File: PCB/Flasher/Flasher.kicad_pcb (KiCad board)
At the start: 2 copper layers, 70 x 70 mm, 48 parts, among them J1 1x5, J2 TC2030-USB-NL, J3 Reset, Q1 BSS138PS, U1 TPS562246, U4 ESP32-S3-MINI-1

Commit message: Start PCb
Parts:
- removed D2, D3: ~, RevK:DFN1006-2L
- removed D4: D, RevK:D_0402
- removed J1: 1x5, RevK:JST_EH_S5B-EH_1x05_P2.50mm_Horizontal
- removed J2: TC2030-USB-NL, RevK:Tag-Connect_TC2030-IDC-NL_2x03_P1.27mm_Vertical
- removed Q1: BSS138PS, RevK:SOT-363_SC-70-6
- removed R1, R2: 10k, RevK:R_0201
- removed TP1: TestPoint, RevK:1x2-Hole
- removed V1, V2: ~, RevK:VCUT70N
- J3, TP10, TP2, TP3, TP4, TP5, TP6, TP7, TP8, TP9, V6: moved to F.Cu
- moved J3 69.7 mm to (195.2, 40.9), turned to 0 degrees
- moved FID3 67.6 mm to (190.2, 44.7)
- moved U4 65.4 mm to (185.6, 31.0), turned to 0 degrees
- moved FID2 62.1 mm to (190.2, 41.2)
- moved R8 54.0 mm to (187.5, 43.1), turned to 0 degrees
- moved R6 54.0 mm to (187.5, 41.6), turned to 0 degrees
- moved R5 53.6 mm to (187.5, 40.1), turned to 0 degrees
- moved C2 53.3 mm to (182.0, 41.6), turned to 0 degrees
- moved TP6 52.9 mm to (176.6, 43.9)
- moved TP8 52.5 mm to (179.6, 40.9)
- moved TP5 51.8 mm to (176.6, 40.9)
- moved C19 51.8 mm to (185.7, 41.6), turned to 0 degrees
- moved C18 51.5 mm to (185.7, 40.1), turned to 0 degrees
- moved TP4 50.5 mm to (173.6, 46.9)
- moved C1 50.2 mm to (182.0, 40.1), turned to 0 degrees
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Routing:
- net +3.3V: track 66.0 -> 0.00 mm, vias 6 -> 0
- net D+: track 44.5 -> 0.00 mm, vias 3 -> 0
- net Net-(J1-Pin_3): track 43.6 -> 0.00 mm
- net D-: track 40.2 -> 0.00 mm, vias 3 -> 0
- net DC: track 38.8 -> 0.00 mm, vias 3 -> 0
- net Net-(D4-K): track 36.0 -> 0.00 mm, vias 4 -> 0
- net RST: track 19.8 -> 0.00 mm, vias 2 -> 0
- net GND: track 10.8 -> 0.00 mm, vias 52 -> 0
- net SW: track 9.82 -> 0.00 mm, vias 2 -> 0
- net RX: track 8.62 -> 0.00 mm, vias 1 -> 0
- net Net-(J3-Pin_2): track 7.03 -> 0.00 mm, vias 1 -> 0
- net TX: track 6.23 -> 0.00 mm, vias 1 -> 0
- net FB: track 2.64 -> 0.00 mm
- net LED: track 2.56 -> 0.00 mm
- net Net-(J1-Pin_1): track 2.22 -> 0.00 mm
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- removed copper zone on B.Cu, net GND
- removed copper zone on F.Cu, net GND
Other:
- board text removed: "${CURRENT_DATE}"
- board text removed: "+"
- board text removed: "-"
- board text removed: "1"
- board text removed: "12V"
- board text removed: "21"
- board text removed: "3"
- board text removed: "34"
- board text removed: "3V3"
- board text removed: "47"
- board text removed: "48"
- board text removed: "5"
- board text removed: "5V"
- board text removed: "6 V-cuts"
- board text removed: "<"
- board text removed: ">"
- board text removed: "A"
- board text removed: "D+"
- board text removed: "D-"
- board text removed: "Designed by RevK www.me.uk"
- board text removed: "EN"
- board text removed: "F"
- board text removed: "Made in China for Andrews & Arnold Ltd"
- board text removed: "RX"
- board text removed: "S21"
- board text removed: "TX"
- board text removed: "U"
- board text removed: "aikin"
- board text removed: "aikin.uk"
- board text removed: "www.f"
- board text removed: "®"
- board text removed: "⏚"

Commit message: Parts
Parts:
- removed C17: 22uF 25V, RevK:C_0805
- removed C18: 100nF, RevK:C_0201
- removed C19: 18pF, RevK:C_0201
- removed FID3: Fiducial, Fiducial:Fiducial_1mm_Mask2mm
- removed TP10, TP2, TP3, TP4, TP5, TP6, TP7, TP8, TP9: TestPoint, RevK:PAD-2mm
- removed V5, V6: ~, RevK:VCUT70N
- added C10: 100nF, RevK:C_0201, F.Cu at (197.9, 49.8)
- added C11: 100nF, RevK:C_0201, F.Cu at (199.8, 46.8)
- added C12: 100nF, RevK:C_0201, F.Cu at (199.8, 48.3)
- added C13: 100nF, RevK:C_0402, F.Cu at (203.9, 52.8)
- added C14: 100nF, RevK:C_0201, F.Cu at (175.2, 58.5)
- added C8: 100nF, RevK:C_0201, F.Cu at (197.9, 46.8)
- added C9: 100nF, RevK:C_0201, F.Cu at (197.9, 48.3)
- added D10: XL-1010RGBC-WS2812B, RevK:SMD1010, F.Cu at (214.1, 53.1)
- added D2: XL-1010RGBC-WS2812B, RevK:SMD1010, F.Cu at (209.4, 47.5)
- added D3: XL-1010RGBC-WS2812B, RevK:SMD1010, F.Cu at (211.7, 47.5)
- added D4: XL-1010RGBC-WS2812B, RevK:SMD1010, F.Cu at (214.1, 47.5)
- added D5: XL-1010RGBC-WS2812B, RevK:SMD1010, F.Cu at (209.4, 50.3)
- added D6: XL-1010RGBC-WS2812B, RevK:SMD1010, F.Cu at (211.7, 50.3)
- added D7: XL-1010RGBC-WS2812B, RevK:SMD1010, F.Cu at (214.1, 50.3)
- added D8: XL-1010RGBC-WS2812B, RevK:SMD1010, F.Cu at (209.4, 53.1)
- added D9: XL-1010RGBC-WS2812B, RevK:SMD1010, F.Cu at (211.7, 53.1)
- added FID1: Fiducial, Fiducial:Fiducial_1mm_Mask2mm, F.Cu at (198.8, 52.4)
- added J1: Reset, RevK:AA-Pad, F.Cu at (188.0, 47.6)
- added J2: Wago, RevK:WAGO-2060-453-998-404, F.Cu at (179.6, 48.8)
- added J4: USB-C-Socket-V, RevK:USB-C-Socket-H, F.Cu at (211.2, 61.8)
- added J5: TF_PUSH, RevK:TF_PUSH, F.Cu at (206.9, 80.4)
- added R1: 150k 1%, RevK:R_0201, F.Cu at (199.8, 49.8)
- added R10: 27R, RevK:R_0201, F.Cu at (216.7, 73.5)
- added R11: 10K, RevK:R_0201, F.Cu at (216.7, 75.0)
- added R12: 10K, RevK:R_0201, F.Cu at (216.7, 76.5)
- added R13: 10K, RevK:R_0201, F.Cu at (216.7, 78.0)
- added R14: 10K, RevK:R_0201, F.Cu at (216.7, 79.5)
- added R15: 10K, RevK:R_0201, F.Cu at (216.7, 81.0)
- added R2: 10K, RevK:R_0201, F.Cu at (201.6, 46.8)
- added R4: 33k 1%, RevK:R_0201, F.Cu at (201.6, 48.3)
- added R7: 5K1, RevK:R_0201, F.Cu at (201.6, 49.8)
- added R9: 27R, RevK:R_0201, F.Cu at (216.7, 72.0)
- added U2: TPS562246, RevK:SOT-563, F.Cu at (204.5, 47.6)
- added U3: FT231XQ, RevK:QFN-20-1EP_4x4mm_P0.5mm_EP2.5x2.5mm, F.Cu at (194.1, 49.0)
- added V1: ~, RevK:VCUT70N, F.Cu at (209.4, 37.2)
- added V2: ~, RevK:VCUT70N, F.Cu at (209.4, 39.7)
- C1: value 100nF -> 22uF 25V; footprint RevK:C_0201 -> RevK:C_0805
- C15: value 47uF 6V -> 100nF; footprint RevK:C_0805 -> RevK:C_0201
- C16: value 100nF 25V -> 100nF; footprint RevK:C_0402 -> RevK:C_0201
- C2: value 100nF -> 100nF 25V; footprint RevK:C_0201 -> RevK:C_0402
- C4: value 100nF -> 1uF
- C6: value 1uF -> 18pF
- C7: value 100nF -> 47uF 6V; footprint RevK:C_0201 -> RevK:C_0805
- J3: value Reset -> Wago; footprint RevK:AA-Pad -> RevK:WAGO-2060-453-998-404
- R3: value 10K -> 150k 1%
- R5, R6: value 150k 1% -> 10K
- R8: value 33k 1% -> 5K1
- U1: value TPS562246 -> ESP32-S3-MINI-1; footprint RevK:SOT-563 -> RevK:ESP32-S3-MINI-1
- U4: value ESP32-S3-MINI-1 -> TPS22916CNYFPR; footprint RevK:ESP32-S3-MINI-1 -> RevK:WCSP-4-0.78x0.78
- moved V3 96.4 mm to (209.5, 32.0)
- moved V4 96.4 mm to (209.5, 34.4)
- moved U4 50.2 mm to (175.7, 80.2)
- moved U1 32.3 mm to (187.6, 82.2)
- moved C3 21.1 mm to (182.8, 70.4)
- moved C1 21.1 mm to (181.4, 61.2)
- moved C2 21.1 mm to (181.4, 62.8)
- moved C4 21.1 mm to (181.4, 64.2)
- moved C5 21.1 mm to (183.2, 61.2)
- moved C6 21.1 mm to (183.2, 62.8)
- moved C7 21.1 mm to (183.2, 64.2)
- moved D1 21.1 mm to (185.2, 74.0)
- moved FID2 21.1 mm to (189.6, 62.3)
- moved J3 21.1 mm to (194.6, 62.0)
- moved L1 21.1 mm to (174.5, 72.6)
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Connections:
- C1 pad 1: GND -> DC
- C1 pad 2: +3.3V -> GND
- C16 pad 1: DC -> +3.3V
- C2 pad 1: GND -> DC
- C2 pad 2: +3.3V -> GND
- C4 pad 1: GND -> RST
- C4 pad 2: +3.3V -> GND
- C5 pad 1: GND -> BST
- C5 pad 2: +3.3V -> SW
- C6 pad 1: RST -> FB
- C6 pad 2: GND -> +3.3V
- C7 pad 1: GND -> +3.3V
- C7 pad 2: +3.3V -> GND
- D1 pad 1: unconnected-(D1-O-Pad1) -> Net-(D1-O)
- J3 pad 1: GND -> Net-(J3-Pin_1)
- J3 pad 2: Net-(J3-Pin_2) -> Net-(J2-Pin_3)
- R3 pad 2: RST -> FB
- R5 pad 1: EN -> +3.3V
- R5 pad 2: DC -> SDCD
- R6 pad 2: FB -> SDDAT1
- R8 pad 1: FB -> GND
- R8 pad 2: GND -> Net-(J4-CC2)
- U1 pad 1: DC -> GND
- U1 pad 2: SW -> GND
- U1 pad 3: GND -> +3.3V
- U1 pad 4: BST -> GPIO0
- U1 pad 5: EN -> unconnected-(U1-GPIO1-Pad5)
- U1 pad 6: FB -> unconnected-(U1-GPIO2-Pad6)

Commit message: Started placement
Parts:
- removed FID1, FID2: Fiducial, Fiducial:Fiducial_1mm_Mask2mm
- removed V1, V4: ~, RevK:VCUT70N
- moved D4 94.5 mm to (124.0, 76.0)
- moved D3 94.1 mm to (122.0, 76.0)
- moved D2 93.8 mm to (120.0, 76.0)
- moved R15 92.2 mm to (125.0, 71.5), turned to -90 degrees
- moved R14 90.6 mm to (126.5, 71.5), turned to -90 degrees
- moved R13 89.0 mm to (128.0, 71.5), turned to -90 degrees
- moved D7 87.9 mm to (130.0, 76.0)
- moved D6 87.6 mm to (128.0, 76.0)
- moved R12 87.4 mm to (129.5, 71.5), turned to -90 degrees
- moved D5 87.3 mm to (126.0, 76.0)
- moved J3 86.6 mm to (108.5, 71.5)
- moved R11 85.8 mm to (131.0, 71.5), turned to -90 degrees
- moved R10 84.2 mm to (132.5, 71.5), turned to -90 degrees
- moved V2 83.7 mm to (135.0, 78.0), turned to 180 degrees
- moved R9 82.7 mm to (134.0, 71.5), turned to -90 degrees
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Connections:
- J2 pad 3: Net-(J2-Pin_3) -> LOOP
- J3 pad 2: Net-(J2-Pin_3) -> LOOP
- U1 pad 14: unconnected-(U1-GPIO10-Pad14) -> LOOP
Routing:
- added copper zone on B.Cu, net GND
- added copper zone on F.Cu, net GND

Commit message: New tweaks
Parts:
- added D11: XL-1010RGBC-WS2812B, RevK:SMD1010, F.Cu at (120.5, 53.5)
- added U5: TPS22916CNYFPR, RevK:WCSP-4-0.78x0.78, F.Cu at (118.3, 54.2)
- C13: footprint RevK:C_0402 -> RevK:C_0201
- J1: moved to B.Cu
- J2, J3: footprint RevK:WAGO-2060-453-998-404 -> RevK:WAGO-2060-453-998-404-S
- moved R6 34.8 mm to (132.5, 71.1), turned to 90 degrees
- moved R10 33.7 mm to (166.2, 70.8)
- moved R5 33.6 mm to (133.6, 71.1), turned to 90 degrees
- moved R9 31.6 mm to (165.6, 70.8)
- moved C12 25.7 mm to (128.1, 71.1), turned to 90 degrees
- moved R8 19.7 mm to (165.8, 55.4), turned to 180 degrees
- moved D1 19.5 mm to (137.4, 74.4)
- moved C8 18.7 mm to (136.0, 59.2), turned to -90 degrees
- moved C11 18.0 mm to (130.3, 71.1), turned to -90 degrees
- moved R2 17.5 mm to (155.4, 58.4), turned to -90 degrees
- moved C7 17.5 mm to (153.1, 75.5), turned to 180 degrees
- moved C16 17.0 mm to (133.8, 73.2), turned to 90 degrees
- moved D10 16.6 mm to (119.4, 74.4)
- moved D2 15.5 mm to (135.4, 74.4)
- moved J2 12.8 mm to (110.0, 71.2)
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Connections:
- net Net-(J3-Pin_1) renamed VOUT
- net PWR renamed PWR5
- C1 pad 1: DC -> VBUS
- C2 pad 1: DC -> VBUS
- C3 pad 1: DC -> VBUS
- D10 pad 1: unconnected-(D10-O-Pad1) -> Net-(D10-O)
- R1 pad 2: DC -> VBUS
- U1 pad 10: unconnected-(U1-GPIO6-Pad10) -> SDDAT0
- U1 pad 11: unconnected-(U1-GPIO7-Pad11) -> SDDAT1
- U1 pad 12: unconnected-(U1-GPIO8-Pad12) -> SDCD
- U1 pad 13: unconnected-(U1-GPIO9-Pad13) -> PWR3
- U1 pad 16: SDDAT2 -> LED
- U1 pad 17: SDDAT3 -> unconnected-(U1-GPIO13-Pad17)
- U1 pad 18: SDCMD -> unconnected-(U1-GPIO14-Pad18)
- U1 pad 19: SDCLK -> unconnected-(U1-GPIO15-Pad19)
- U1 pad 20: SDDAT0 -> unconnected-(U1-GPIO16-Pad20)
- U1 pad 21: SDDAT1 -> unconnected-(U1-GPIO17-Pad21)
- U1 pad 22: SDCD -> unconnected-(U1-GPIO18-Pad22)
- U1 pad 27: LED -> unconnected-(U1-GPIO47-Pad27)
- U1 pad 6: unconnected-(U1-GPIO2-Pad6) -> SDDAT2
- U1 pad 7: unconnected-(U1-GPIO3-Pad7) -> SDDAT3
- U1 pad 8: unconnected-(U1-GPIO4-Pad8) -> SDCMD
- U1 pad 9: unconnected-(U1-GPIO5-Pad9) -> SDCLK
- U2 pad 1: DC -> VBUS
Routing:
- net +3.3V: track 0.00 -> 136.1 mm, vias 0 -> 6
- net VBUS: track 0.00 -> 104.0 mm, vias 0 -> 2
- net LOOP: track 0.00 -> 79.9 mm, vias 0 -> 4
- net D-: track 0.00 -> 65.1 mm
- net D+: track 0.00 -> 57.1 mm
- net GPIO0: track 0.00 -> 46.8 mm, vias 0 -> 2
- net PWR3: track 0.00 -> 32.9 mm, vias 0 -> 2
- net PWR5: track 0.00 -> 32.6 mm, vias 0 -> 2
- net RST: track 0.00 -> 31.1 mm, vias 0 -> 2
- net TXD: track 0.00 -> 26.1 mm, vias 0 -> 2
- net RXD: track 0.00 -> 23.2 mm, vias 0 -> 2
- net Net-(D10-O): track 0.00 -> 22.5 mm
- net Net-(J4-D+-PadA6): track 0.00 -> 20.2 mm, vias 0 -> 2
- net SDDAT2: track 0.00 -> 19.1 mm
- net SDDAT3: track 0.00 -> 17.9 mm
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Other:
- board text added: "+"
- board text added: "-"
- board text added: "1"
- board text added: "10"
- board text added: "19"
- board text added: "2"
- board text added: "2 3 4 5 6 7 8"
- board text added: "20"
- board text added: "21"
- board text added: "3"
- board text added: "4"
- board text added: "5"
- board text added: "6"
- board text added: "9 11 12"
- board text added: "A"
- board text added: "DAT2 DAT3 CMD CLK DAT0 DAT1 CD"
- board text added: "Flasher"
- board text added: "Made in China for Andrews&Arnold Ltd ${CURRENT_DATE} Code flasher"
- board text added: "PWR"
- board text added: "PWR3 PWR5 LED"
- board text added: "TC2030"
- board text added: "U"
- board text added: "www.me.uk"

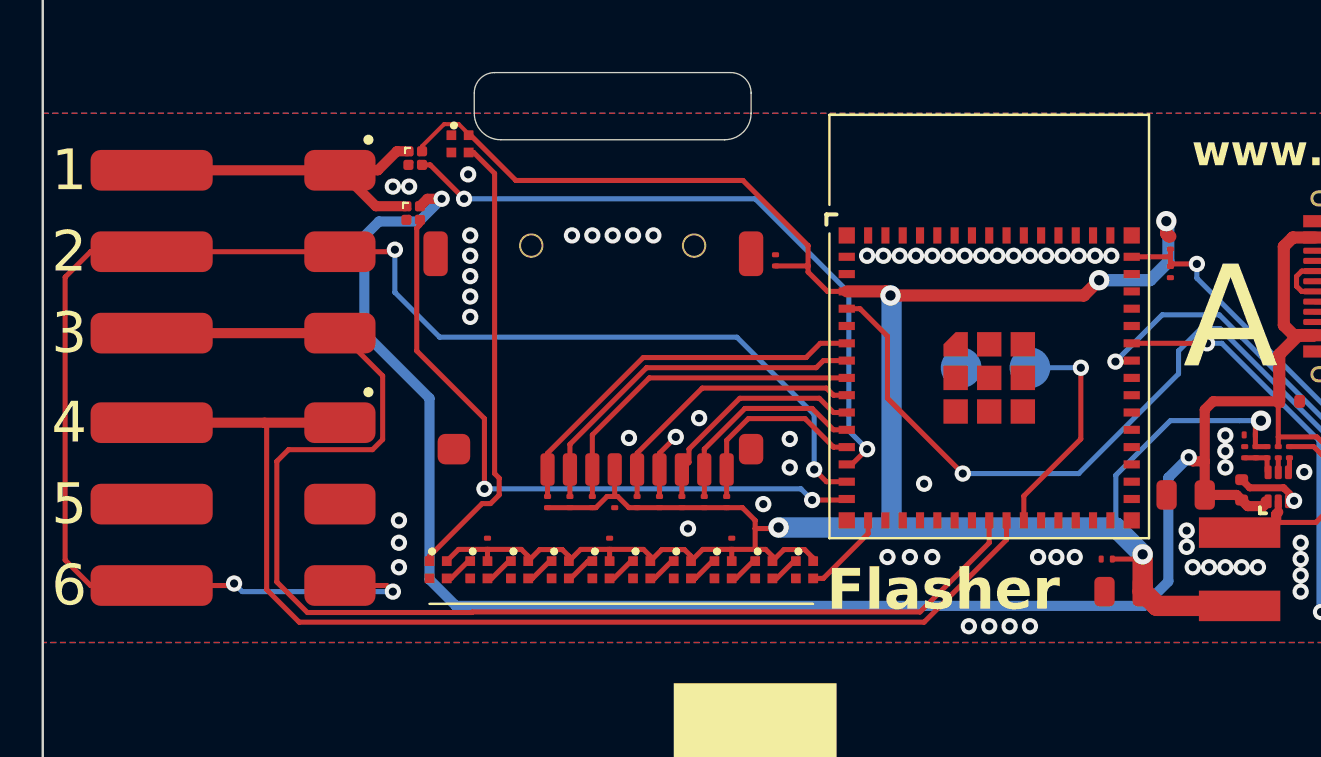
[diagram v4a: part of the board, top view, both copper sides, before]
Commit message: New sockets
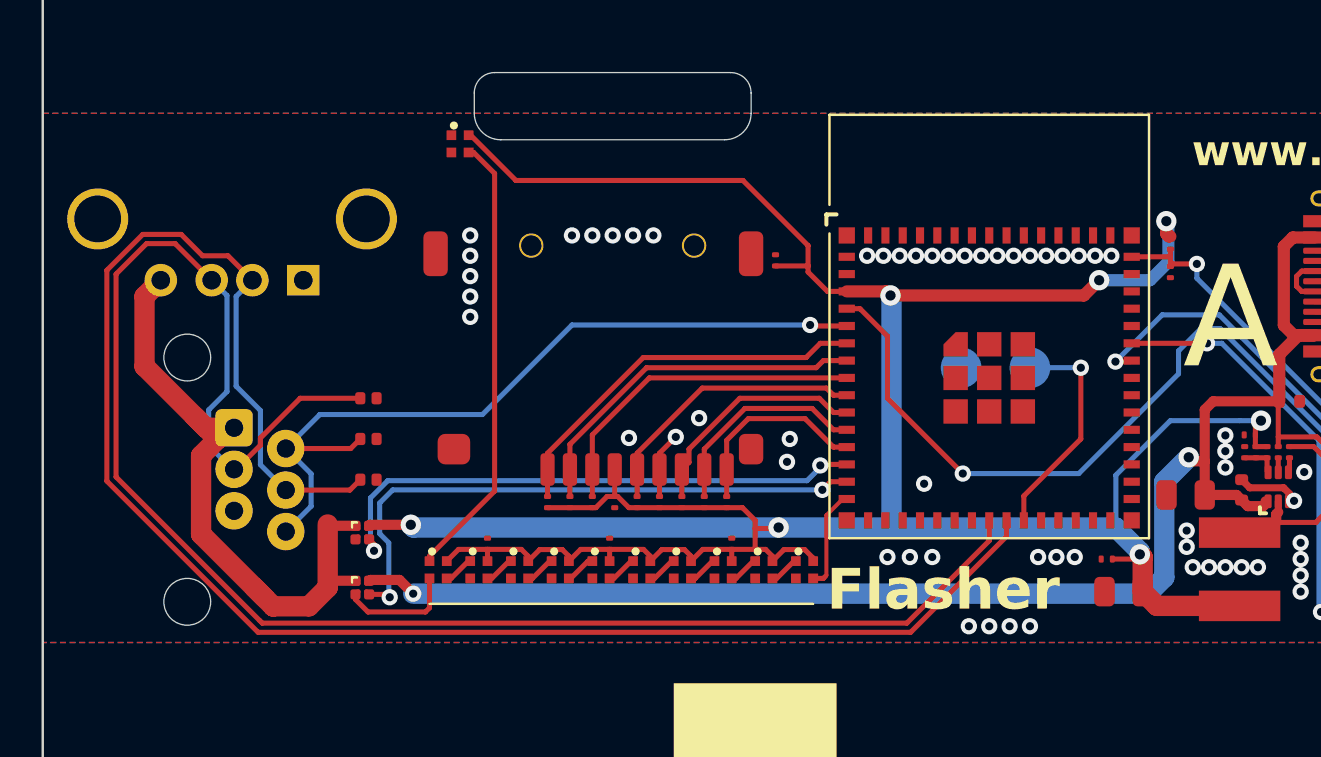
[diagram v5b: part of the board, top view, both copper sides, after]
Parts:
- added D12: ~, RevK:DFN1006-2L, F.Cu at (116.0, 66.0)
- added D13: ~, RevK:DFN1006-2L, F.Cu at (116.0, 70.0)
- added D14: ~, RevK:DFN1006-2L, F.Cu at (116.0, 68.0)
- J2: value Wago -> RJ12; footprint RevK:WAGO-2060-453-998-404-S -> RevK:RJ12_Horizontal
- J3: value Wago -> USB; footprint RevK:WAGO-2060-453-998-404-S -> RevK:USB_A_Horizontal
- moved U5 18.6 mm to (115.7, 72.6)
- moved U4 18.6 mm to (115.7, 75.3)
- moved J2 3.14 mm to (107.1, 70.0), turned to -90 degrees
- moved J3 1.76 mm to (109.3, 57.2), turned to 180 degrees
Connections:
- J2 pad 1: D+ -> VOUT
- J2 pad 2: GND -> LOOP
- J2 pad 3: LOOP -> D-
- J3 pad 1: VOUT -> GND
- J3 pad 2: LOOP -> D+
- U1 pad 14: LOOP -> PWR5
- U1 pad 15: PWR5 -> LED
- U1 pad 16: LED -> unconnected-(U1-GPIO12-Pad16)
- U1 pad 5: unconnected-(U1-GPIO1-Pad5) -> LOOP
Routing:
- net LOOP: track 79.9 -> 39.1 mm, vias 4 -> 1
- net D+: track 57.1 -> 84.7 mm
- net VBUS: track 104.0 -> 82.2 mm
- net D-: track 65.1 -> 82.8 mm
- net +3.3V: track 136.1 -> 152.9 mm, vias 6 -> 7
- net VOUT: track 17.0 -> 31.6 mm
- net GND: track 16.2 -> 21.9 mm, vias 66 -> 58
- net PWR3: track 32.9 -> 27.5 mm
- net PWR5: track 32.6 -> 29.3 mm
- net LED: track 4.26 -> 4.79 mm
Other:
- board text added: "9 10 11"
- board text removed: "10"
- board text removed: "2"
- board text removed: "3"
- board text removed: "4"
- board text removed: "5"
- board text removed: "6"
- board text removed: "9 11 12"
- board text removed: "PWR"

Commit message: Board ready
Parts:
- added SW1: SW_Push_DPDT, RevK:SW_Push_DPDT, F.Cu at (130.9, 73.0)
- moved D10 18.5 mm to (121.0, 56.0), turned to -90 degrees
- moved C10 16.9 mm to (142.5, 60.1), turned to 90 degrees
- moved D1 16.4 mm to (121.0, 74.0), turned to -90 degrees
- moved D9 16.4 mm to (121.0, 58.0), turned to -90 degrees
- moved C14 14.7 mm to (122.3, 58.5), turned to 0 degrees
- moved D2 14.6 mm to (121.0, 72.0), turned to -90 degrees
- moved D8 14.6 mm to (121.0, 60.0), turned to -90 degrees
- moved D3 13.2 mm to (121.0, 70.0), turned to -90 degrees
- moved D7 13.2 mm to (121.0, 62.0), turned to -90 degrees
- moved D4 12.2 mm to (121.0, 68.0), turned to -90 degrees
- moved D6 12.2 mm to (121.0, 64.0), turned to -90 degrees
- moved D5 11.9 mm to (121.0, 66.0), turned to -90 degrees
- moved C16 11.9 mm to (122.3, 70.5), turned to 0 degrees
- moved C15 10.3 mm to (122.3, 64.5), turned to 0 degrees
- moved C12 6.75 mm to (134.6, 69.1)
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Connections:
- U1 pad 16: unconnected-(U1-GPIO12-Pad16) -> BTN
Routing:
- net +3.3V: track 152.9 -> 181.6 mm, vias 7 -> 6
- net LED: track 4.79 -> 32.7 mm, vias 0 -> 2
- net BTN: track 0.00 -> 19.1 mm
- net Net-(D10-O): track 22.1 -> 7.63 mm
- net GND: track 21.9 -> 35.4 mm, vias 58 -> 14
- net PWR3: track 27.5 -> 38.0 mm
- net VOUT: track 31.6 -> 22.3 mm
- net D-: track 82.8 -> 73.8 mm
- net RXD: track 23.2 -> 30.2 mm
- net RST: track 31.1 -> 36.9 mm
- net GPIO0: track 46.8 -> 42.1 mm
- net Net-(J4-D+-PadA6): track 20.2 -> 16.1 mm
- net Net-(J1-Pin_2): track 11.2 -> 7.17 mm
- net VBUS: track 82.2 -> 78.2 mm, vias 2 -> 0
- net LOOP: track 39.1 -> 42.8 mm, vias 1 -> 2
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- added copper zone on F.Cu, net VBUS
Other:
- board text added: "12"
